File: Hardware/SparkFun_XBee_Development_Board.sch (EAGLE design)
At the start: 80 parts, among them J4 QWIIC_RIGHT_ANGLE, Q2 3.1A/30V/105mΩ, U1 FSUSB30MUX_MSOP10, U2 AP63203, U3 ESD Diode, U4 MCP73831, U5 ESD Diode, U7 FT231XS

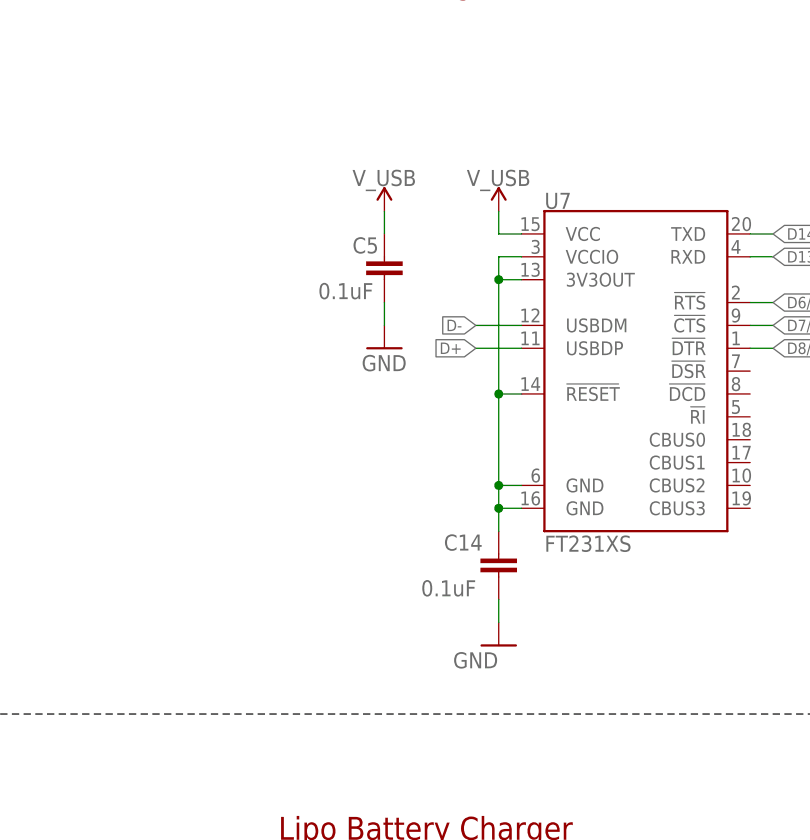
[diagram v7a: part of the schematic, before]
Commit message: Moves ground pin nets to the bottom of the decoupling cap
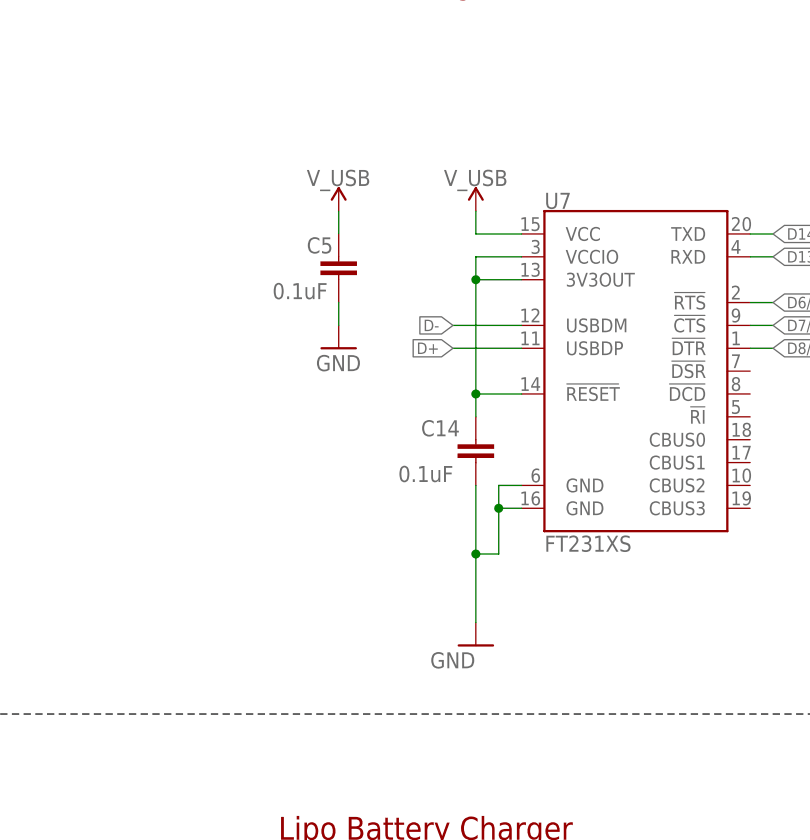
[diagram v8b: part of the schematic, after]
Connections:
- net GND: now also U7.GND@16, U7.GND@6
- net N$18: no longer U7.GND@16, U7.GND@6
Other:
- moved on the sheet: C14, C5
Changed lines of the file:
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@@
 <attribute name="VALUE" x="375.92" y="207.772" size="1.778" layer="96" align="top-left"/>
 </instance>
-<instance part="C14" gate="G$1" x="370.84" y="203.2" smashed="yes">
-<attribute name="NAME" x="364.744" y="206.121" size="1.778" layer="95" font="vector"/>
-<attribute name="VALUE" x="362.204" y="201.041" size="1.778" layer="96" font="vector"/>
-</instance>
-<instance part="C5" gate="G$1" x="358.14" y="236.22" smashed="yes">
-<attribute name="NAME" x="354.584" y="239.141" size="1.778" layer="95" font="vector"/>
-<attribute name="VALUE" x="350.774" y="234.061" size="1.778" layer="96" font="vector"/>
-</instance>
-<instance part="GND30" gate="1" x="358.14" y="228.6" smashed="yes">
-<attribute name="VALUE" x="355.6" y="226.06" size="1.778" layer="96" font="vector"/>
-</instance>
-<instance part="GND32" gate="1" x="370.84" y="195.58" smashed="yes">
-<attribute name="VALUE" x="365.76" y="193.04" size="1.778" layer="96" font="vector"/>
+<instance part="C14" gate="G$1" x="368.3" y="215.9" smashed="yes">
+<attribute name="NAME" x="362.204" y="218.821" size="1.778" layer="95" font="vector"/>
+<attribute name="VALUE" x="359.664" y="213.741" size="1.778" layer="96" font="vector"/>
+</instance>
+<instance part="C5" gate="G$1" x="353.06" y="236.22" smashed="yes">
+<attribute name="NAME" x="349.504" y="239.141" size="1.778" layer="95" font="vector"/>
+<attribute name="VALUE" x="345.694" y="234.061" size="1.778" layer="96" font="vector"/>
+</instance>
+<instance part="GND30" gate="1" x="353.06" y="228.6" smashed="yes">
+<attribute name="VALUE" x="350.52" y="226.06" size="1.778" layer="96" font="vector"/>
+</instance>
+<instance part="GND32" gate="1" x="368.3" y="195.58" smashed="yes">
+<attribute name="VALUE" x="363.22" y="193.04" size="1.778" layer="96" font="vector"/>
 </instance>
 <instance part="L1" gate="G$1" x="261.62" y="142.24" smashed="yes" rot="R90">
@@
 <attribute name="NAME" x="308.61" y="42.926" size="1.778" layer="95" font="vector" rot="R180" align="center"/>
 </instance>
-<instance part="SUPPLY22" gate="G$1" x="370.84" y="243.84" smashed="yes">
-<attribute name="VALUE" x="370.84" y="246.634" size="1.778" layer="96" font="vector" align="bottom-center"/>
-</instance>
-<instance part="SUPPLY6" gate="G$1" x="358.14" y="243.84" smashed="yes">
-<attribute name="VALUE" x="358.14" y="246.634" size="1.778" layer="96" font="vector" align="bottom-center"/>
+<instance part="SUPPLY22" gate="G$1" x="368.3" y="243.84" smashed="yes">
+<attribute name="VALUE" x="368.3" y="246.634" size="1.778" layer="96" font="vector" align="bottom-center"/>
+</instance>
+<instance part="SUPPLY6" gate="G$1" x="353.06" y="243.84" smashed="yes">
+<attribute name="VALUE" x="353.06" y="246.634" size="1.778" layer="96" font="vector" align="bottom-center"/>
 </instance>
 </instances>
@@
 <segment>
 <pinref part="C5" gate="G$1" pin="2"/>
-<wire x1="358.14" y1="231.14" x2="358.14" y2="233.68" width="0.1524" layer="91"/>
+<wire x1="353.06" y1="231.14" x2="353.06" y2="233.68" width="0.1524" layer="91"/>
 <pinref part="GND30" gate="1" pin="GND"/>
 </segment>
 <segment>
+<pinref part="GND32" gate="1" pin="GND"/>
+<pinref part="U7" gate="U$1" pin="GND@6"/>
+<wire x1="373.38" y1="213.36" x2="370.84" y2="213.36" width="0.1524" layer="91"/>
 <pinref part="C14" gate="G$1" pin="2"/>
-<wire x1="370.84" y1="200.66" x2="370.84" y2="198.12" width="0.1524" layer="91"/>
-<pinref part="GND32" gate="1" pin="GND"/>
+<wire x1="368.3" y1="213.36" x2="368.3" y2="205.74" width="0.1524" layer="91"/>
+<pinref part="U7" gate="U$1" pin="GND@16"/>
+<wire x1="368.3" y1="205.74" x2="368.3" y2="198.12" width="0.1524" layer="91"/>
+<wire x1="373.38" y1="210.82" x2="370.84" y2="210.82" width="0.1524" layer="91"/>
+<wire x1="370.84" y1="210.82" x2="370.84" y2="205.74" width="0.1524" layer="91"/>
+<wire x1="370.84" y1="205.74" x2="368.3" y2="205.74" width="0.1524" layer="91"/>
+<junction x="368.3" y="205.74"/>
+<wire x1="370.84" y1="213.36" x2="370.84" y2="210.82" width="0.1524" layer="91"/>
+<junction x="370.84" y="210.82"/>
 </segment>
 <segment>
@@
 <pinref part="U7" gate="U$1" pin="VCC"/>
 <pinref part="SUPPLY22" gate="G$1" pin="V_USB"/>
-<wire x1="373.38" y1="241.3" x2="370.84" y2="241.3" width="0.1524" layer="91"/>
-<wire x1="370.84" y1="241.3" x2="370.84" y2="243.84" width="0.1524" layer="91"/>
+<wire x1="373.38" y1="241.3" x2="368.3" y2="241.3" width="0.1524" layer="91"/>
+<wire x1="368.3" y1="241.3" x2="368.3" y2="243.84" width="0.1524" layer="91"/>
 </segment>
 <segment>
 <pinref part="C5" gate="G$1" pin="1"/>
 <pinref part="SUPPLY6" gate="G$1" pin="V_USB"/>
-<wire x1="358.14" y1="241.3" x2="358.14" y2="243.84" width="0.1524" layer="91"/>
+<wire x1="353.06" y1="241.3" x2="353.06" y2="243.84" width="0.1524" layer="91"/>
 </segment>
 </net>
@@
 </segment>
 <segment>
-<wire x1="373.38" y1="228.6" x2="368.3" y2="228.6" width="0.1524" layer="91"/>
-<label x="368.3" y="228.6" size="1.27" layer="95" font="vector" rot="R180" xref="yes"/>
+<wire x1="373.38" y1="228.6" x2="365.76" y2="228.6" width="0.1524" layer="91"/>
+<label x="365.76" y="228.6" size="1.27" layer="95" font="vector" rot="R180" xref="yes"/>
 <pinref part="U7" gate="U$1" pin="USBDP"/>
 </segment>
@@
 </segment>
 <segment>
-<wire x1="373.38" y1="231.14" x2="368.3" y2="231.14" width="0.1524" layer="91"/>
-<label x="368.3" y="231.14" size="1.27" layer="95" font="vector" rot="R180" xref="yes"/>
+<wire x1="373.38" y1="231.14" x2="365.76" y2="231.14" width="0.1524" layer="91"/>
+<label x="365.76" y="231.14" size="1.27" layer="95" font="vector" rot="R180" xref="yes"/>
 <pinref part="U7" gate="U$1" pin="USBDM"/>
 </segment>
@@
 <net name="N$18" class="0">
 <segment>
-<pinref part="U7" gate="U$1" pin="GND@16"/>
 <pinref part="C14" gate="G$1" pin="1"/>
-<wire x1="373.38" y1="210.82" x2="370.84" y2="210.82" width="0.1524" layer="91"/>
-<wire x1="370.84" y1="210.82" x2="370.84" y2="208.28" width="0.1524" layer="91"/>
-<pinref part="U7" gate="U$1" pin="GND@6"/>
-<wire x1="373.38" y1="213.36" x2="370.84" y2="213.36" width="0.1524" layer="91"/>
-<wire x1="370.84" y1="213.36" x2="370.84" y2="210.82" width="0.1524" layer="91"/>
-<junction x="370.84" y="210.82"/>
-<wire x1="370.84" y1="213.36" x2="370.84" y2="223.52" width="0.1524" layer="91"/>
-<junction x="370.84" y="213.36"/>
+<pinref part="U7" gate="U$1" pin="VCCIO"/>
+<wire x1="373.38" y1="238.76" x2="368.3" y2="238.76" width="0.1524" layer="91"/>
+<wire x1="368.3" y1="236.22" x2="368.3" y2="238.76" width="0.1524" layer="91"/>
+<pinref part="U7" gate="U$1" pin="3V3OUT"/>
+<wire x1="373.38" y1="236.22" x2="368.3" y2="236.22" width="0.1524" layer="91"/>
+<junction x="368.3" y="236.22"/>
 <pinref part="U7" gate="U$1" pin="!RESET"/>
-<wire x1="370.84" y1="223.52" x2="373.38" y2="223.52" width="0.1524" layer="91"/>
-<pinref part="U7" gate="U$1" pin="VCCIO"/>
-<wire x1="373.38" y1="238.76" x2="370.84" y2="238.76" width="0.1524" layer="91"/>
-<wire x1="370.84" y1="236.22" x2="370.84" y2="238.76" width="0.1524" layer="91"/>
-<pinref part="U7" gate="U$1" pin="3V3OUT"/>
-<wire x1="373.38" y1="236.22" x2="370.84" y2="236.22" width="0.1524" layer="91"/>
-<wire x1="370.84" y1="223.52" x2="370.84" y2="236.22" width="0.1524" layer="91"/>
-<junction x="370.84" y="223.52"/>
-<junction x="370.84" y="236.22"/>
-</segment>
-</net>
+<wire x1="368.3" y1="223.52" x2="373.38" y2="223.52" width="0.1524" layer="91"/>
+<wire x1="368.3" y1="223.52" x2="368.3" y2="236.22" width="0.1524" layer="91"/>
+<junction x="368.3" y="223.52"/>
+<wire x1="368.3" y1="223.52" x2="368.3" y2="220.98" width="0.1524" layer="91"/>
+</segment>
+</net>
